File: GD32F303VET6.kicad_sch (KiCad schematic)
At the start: 32 parts, among them SW1 SKRPACE010, U6 GD32F303VCT6, Y1 TAXM8M4RDBCCT2T, Y2 XKXGI-SUA-32.768K

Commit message: 重命名为GD32F303VET6四电机驱动控制板
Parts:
- U6: value GD32F303VCT6 -> GD32F303VET6; footprint kicad_api_lib:GD32F303VCT6 -> kicad_api_lib:GD32F303VET6; symbol GD32F303VCT6:GD32F303VCT6_Mulit -> GD32F303VET6:GD32F303VET6_Mulit

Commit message: 更新六层控制板设计及嘉立创生产文件
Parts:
- removed unit 5 of U6
- renumbered C15 to C16, C16 to C17, C17 to C18, C18 to C19, C19 to C20, C20 to C21, C21 to C22, C22 to C23, C23 to C24, C24 to C25, C25 to C26, C26 to C27, C27 to C28, C28 to C29, C29 to C30, C30 to C31, C31 to C32, C32 to C33, C33 to C34, C34 to C35, D5 to D7, R9 to R11, R10 to R12, R11 to R13, R12 to R14
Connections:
- net DIR2_2 is gone; now on net DIR1_2: U6.34 (DIR2)
- net BRAKE1_1: now also U6.44 (BRAKE1)
- net BRAKE1_2: now also U6.32 (BRAKE2)
- net BRAKE1_3: now also U6.83 (BRAKE3); no longer U6.85 (BRAKE1)
- net BRAKE1_4: now also U6.91 (BRAKE4); no longer U6.87 (BRAKE3)
- net CAN_RX: now also U6.81 (CAN_RX); no longer U6.95 (CAN_RX)
- net CAN_TX: now also U6.82 (CAN_TX); no longer U6.96 (CAN_TX)
- net DIR1_1: now also U6.46 (DIR1)
- net DIR1_3: now also U6.84 (DIR3); no longer U6.86 (BRAKE2)
- net DIR1_4: now also U6.95 (DIR4); no longer U6.88 (BRAKE4)
- net FG1_1: now also U6.45 (TIMER0_CH3-FG1); no longer U6.23 (TIMER1_CH0-FG1)
- net FG1_2: now also U6.42 (TIMER0_CH1-FG2); no longer U6.24 (TIMER1_CH1-FG2)
- net FG1_3: now also U6.90 (TIMER2_CH0-FG3); no longer U6.25 (TIMER1_CH2-FG3)
- net FG1_4: now also U6.96 (TIMER10_CH0-FG4); no longer U6.26 (TIMER1_CH3-FG4)
- net RS485_DE: now also U6.24 (RS485_DE); no longer U6.46 (RS485_DE)
- net RS485_RX: now also U6.26 (RS485_RX); no longer U6.48 (RS485_RX)
- net RS485_TX: now also U6.25 (RS485_TX); no longer U6.47 (RS485_TX)
- net USART0_RX: now also U6.69 (USART0_RX)
- net USART0_TX: now also U6.68 (USART0_TX)
- removed net DIR2_1: U6.33 (DIR1)
- no-connect marks 30 -> 2

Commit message: 更新电机控制板原理图与PCB设计
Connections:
- net FG1_1: now also U6.47 (TIMER1_CH2-FG1); no longer U6.45 (TIMER0_CH3-FG1)
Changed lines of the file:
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@@
 			(alternate "PA3")
 		)
-		(pin "45"
+		(pin "47"
 		)
 		(pin "32"
@@
 		(pin "32"
 		)
-		(pin "45"
+		(pin "47"
 		)
 		(pin "15"
@@
 		(pin "96"
 		)
-		(pin "45"
+		(pin "47"
 		)
 		(pin "62"
@@
 			(alternate "PA3")
 		)
-		(pin "45"
+		(pin "47"
 		)
 		(pin "32"

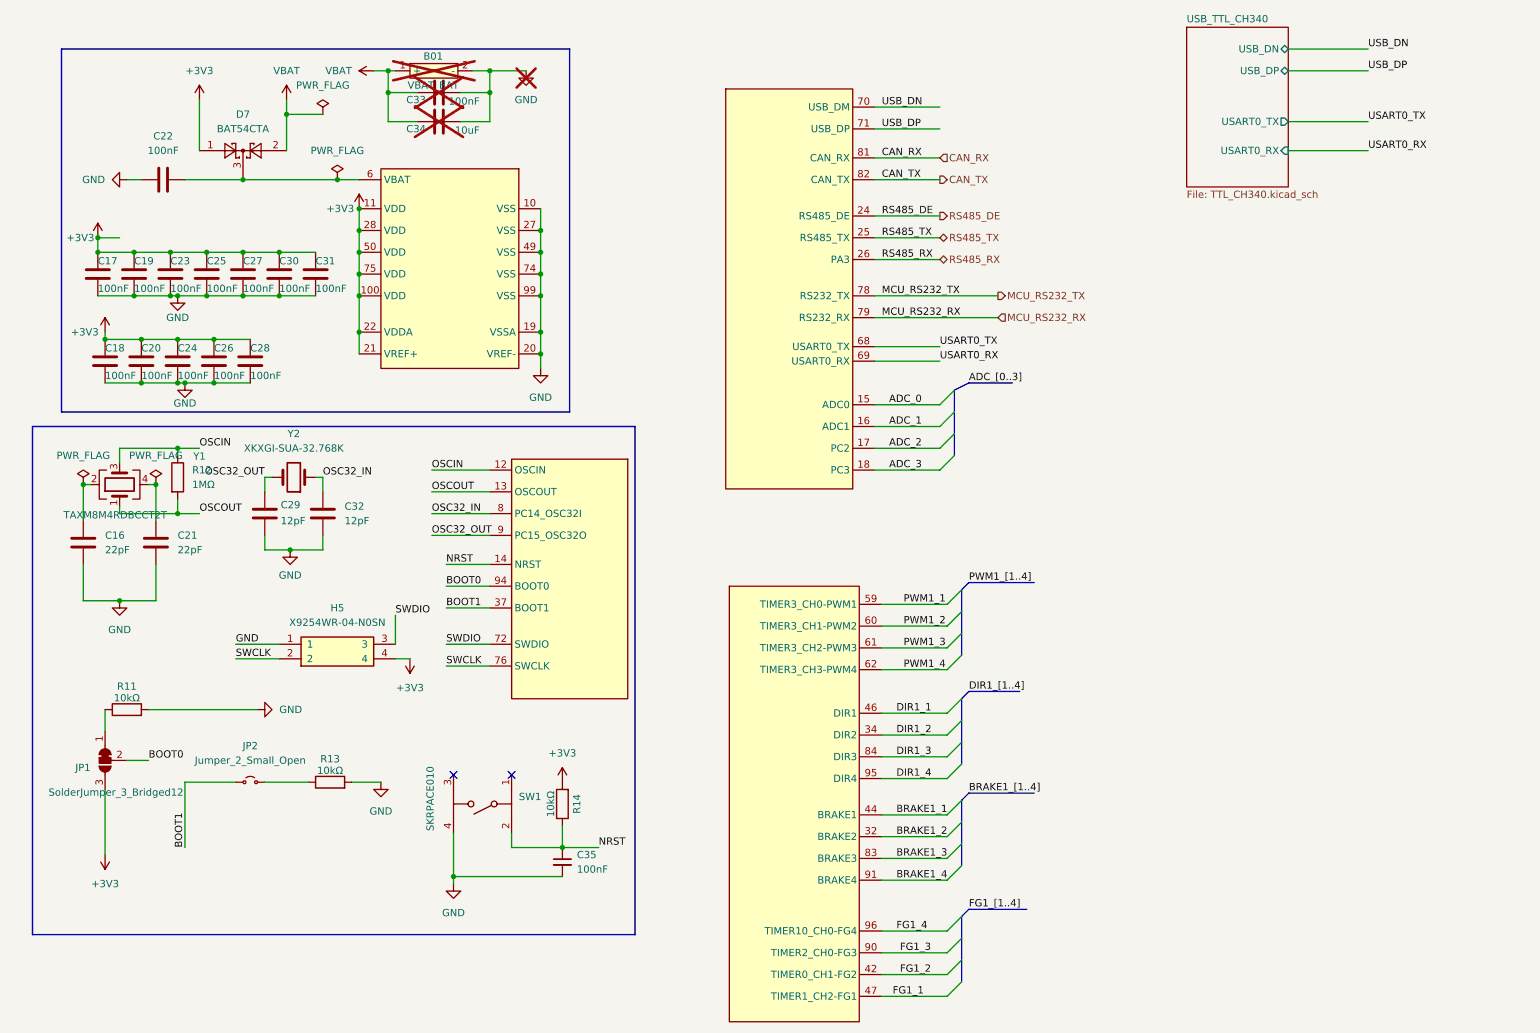
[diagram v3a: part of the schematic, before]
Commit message: 更新六层电机控制板设计与器件库
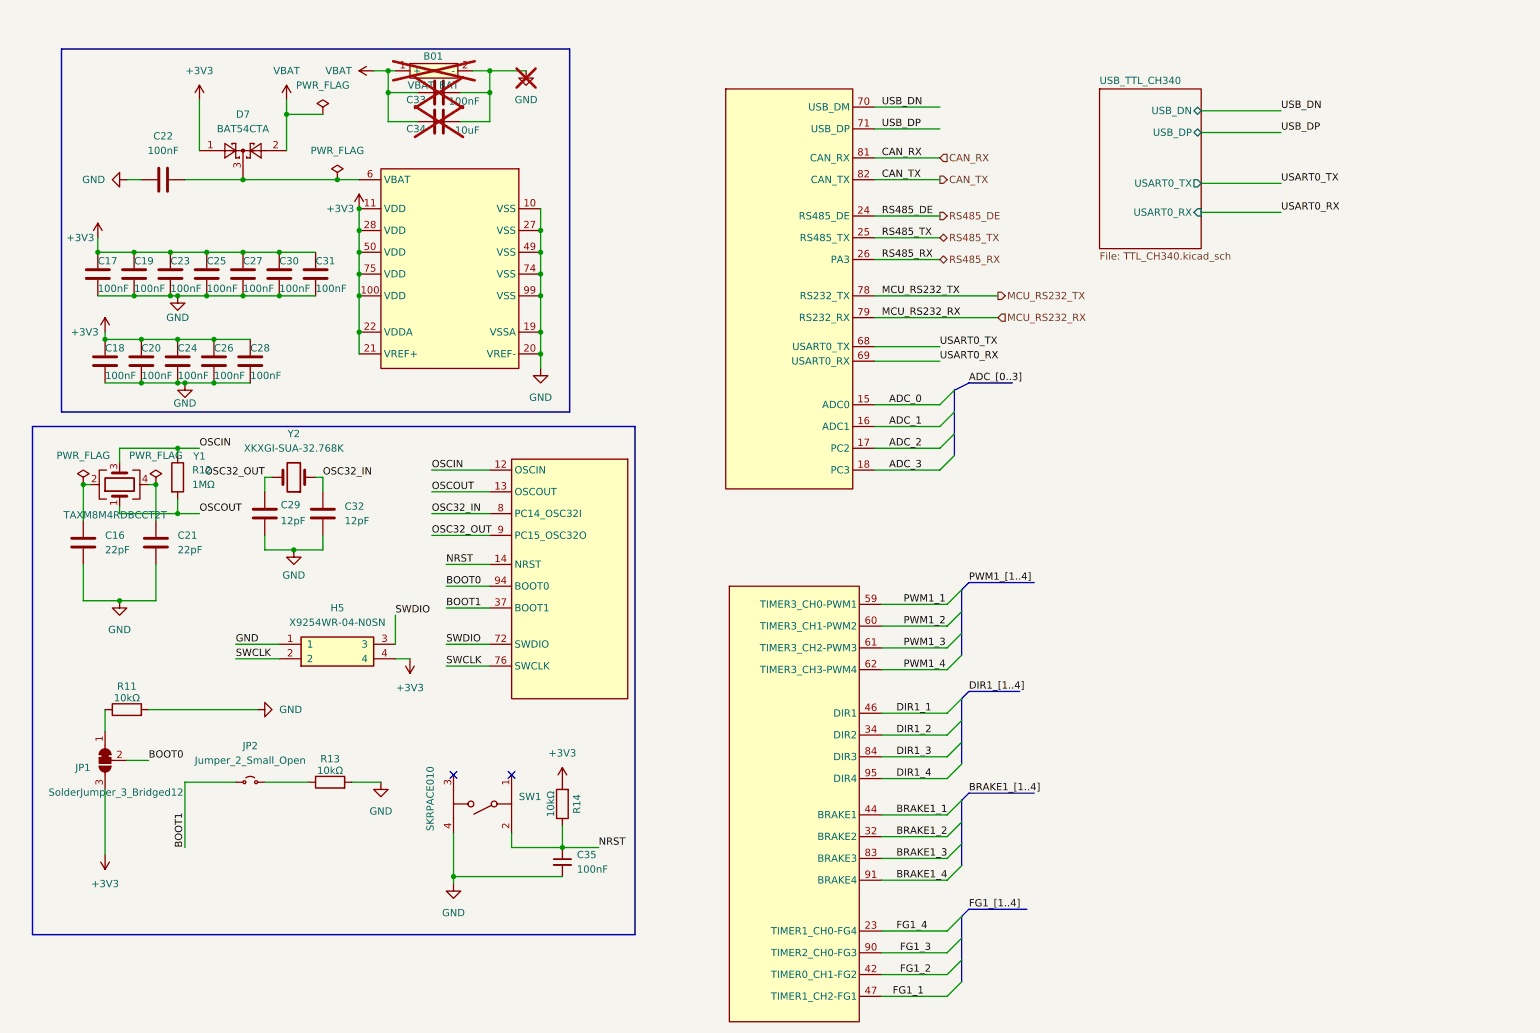
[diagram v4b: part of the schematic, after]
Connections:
- net FG1_4: now also U6.23 (TIMER1_CH0-FG4); no longer U6.96 (TIMER10_CH0-FG4)
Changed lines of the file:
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@@
 	)
 	(junction
+		(at 59.69 113.03)
+		(diameter 0)
+		(color 0 0 0 0)
+	)
+	(junction
 		(at 29.21 121.92)
 		(diameter 0)
@@
 	)
 	(junction
-		(at 25.4 58.42)
-		(diameter 0)
-		(color 0 0 0 0)
-	)
-	(junction
 		(at 93.98 33.02)
 		(diameter 0)
@@
 	)
 	(junction
-		(at 59.055 113.03)
-		(diameter 0)
-		(color 0 0 0 0)
-	)
-	(junction
 		(at 67.31 48.26)
 		(diameter 0)
@@
 	(wire
 		(pts
-			(xy 59.055 113.03) (xy 64.77 113.03)
-		)
-		(stroke
-			(width 0)
-			(type default)
-		)
-	)
-	(wire
-		(pts
 			(xy 34.29 140.97) (xy 53.34 140.97)
 		)
@@
 	(wire
 		(pts
-			(xy 247.65 29.21) (xy 233.68 29.21)
+			(xy 232.41 40.005) (xy 218.44 40.005)
 		)
 		(stroke
@@
 	(wire
 		(pts
-			(xy 54.61 113.03) (xy 59.055 113.03)
+			(xy 54.61 113.03) (xy 59.69 113.03)
 		)
 		(stroke
@@
 	(wire
 		(pts
-			(xy 233.68 25.4) (xy 247.65 25.4)
+			(xy 218.44 36.195) (xy 232.41 36.195)
 		)
 		(stroke
@@
 	(wire
 		(pts
+			(xy 59.69 113.03) (xy 64.77 113.03)
+		)
+		(stroke
+			(width 0)
+			(type default)
+		)
+	)
+	(wire
+		(pts
 			(xy 54.61 153.67) (xy 62.23 153.67)
 		)
@@
 	(wire
 		(pts
-			(xy 233.68 38.1) (xy 247.65 38.1)
+			(xy 218.44 48.895) (xy 232.41 48.895)
 		)
 		(stroke
@@
 	(wire
 		(pts
-			(xy 29.21 58.42) (xy 25.4 58.42)
-		)
-		(stroke
-			(width 0)
-			(type default)
-		)
-	)
-	(wire
-		(pts
 			(xy 87.63 170.18) (xy 106.68 170.18)
 		)
@@
 	(wire
 		(pts
-			(xy 247.65 43.18) (xy 233.68 43.18)
+			(xy 232.41 53.975) (xy 218.44 53.975)
 		)
 		(stroke
@@
 	)
 	(label "USART0_RX"
-		(at 247.65 43.18 0)
+		(at 232.41 53.975 0)
 		(effects
 			(font
@@
 	)
 	(label "USB_DN"
-		(at 247.65 25.4 0)
+		(at 232.41 36.195 0)
 		(effects
 			(font
@@
 	)
 	(label "USB_DP"
-		(at 247.65 29.21 0)
+		(at 232.41 40.005 0)
 		(effects
 			(font
@@
 	)
 	(label "USART0_TX"
-		(at 247.65 38.1 0)
+		(at 232.41 48.895 0)
 		(effects
 			(font
@@
 		(pin "17"
 		)
-		(pin "96"
+		(pin "23"
 		)
 		(pin "42"
@@
 	(symbol
 		(lib_id "power:GND")
-		(at 59.055 113.03 0)
+		(at 59.69 113.03 0)
 		(unit 1)
 		(body_style 1)
@@
 		(fields_autoplaced yes)
 		(property "Reference" "#PWR043"
-			(at 59.055 119.38 0)
+			(at 59.69 119.38 0)
 			(hide yes)
 			(show_name no)
@@
 		)
 		(property "Value" "GND"
-			(at 59.055 117.475 0)
+			(at 59.69 117.475 0)
 			(show_name no)
 			(do_not_autoplace no)
@@
 		)
 		(property "Footprint" ""
-			(at 59.055 113.03 0)
+			(at 59.69 113.03 0)
 			(hide yes)
 			(show_name no)
@@
 		)
 		(property "Datasheet" ""
-			(at 59.055 113.03 0)
+			(at 59.69 113.03 0)
 			(hide yes)
 			(show_name no)
@@
 		)
 		(property "Description" "Power symbol creates a global label with name \"GND\" , ground"
-			(at 59.055 113.03 0)
+			(at 59.69 113.03 0)
 			(hide yes)
 			(show_name no)
@@
 		(pin "70"
 		)
-		(pin "96"
+		(pin "23"
 		)
 		(pin "61"
@@
 		(dnp no)
 		(fields_autoplaced yes)
-		(property "Reference" "#FLG012"
+		(property "Reference" "#FLG013"
 			(at 67.31 46.355 0)
 			(hide yes)
@@
 			(project "GD32F303VET6_4Motor_Control"
 				(path "/54005433-e3aa-4693-8f75-bb73943288d3/ab5b236f-20a8-4993-b87c-2c1c522e6f92"
-					(reference "#FLG012")
+					(reference "#FLG013")
 					(unit 1)
 				)
@@
 		(dnp no)
 		(fields_autoplaced yes)
-		(property "Reference" "#FLG011"
+		(property "Reference" "#FLG012"
 			(at 64.77 34.925 0)
 			(hide yes)
@@
 			(project "GD32F303VET6_4Motor_Control"
 				(path "/54005433-e3aa-4693-8f75-bb73943288d3/ab5b236f-20a8-4993-b87c-2c1c522e6f92"
-					(reference "#FLG011")
+					(reference "#FLG012")
 					(unit 1)
 				)
@@
 		(pin "17"
 		)
-		(pin "96"
+		(pin "23"
 		)
 		(pin "47"
@@
 		(dnp no)
 		(fields_autoplaced yes)
-		(property "Reference" "#FLG09"
+		(property "Reference" "#FLG010"
 			(at 22.86 99.695 0)
 			(hide yes)
@@
 			(project "GD32F303VET6_4Motor_Control"
 				(path "/54005433-e3aa-4693-8f75-bb73943288d3/ab5b236f-20a8-4993-b87c-2c1c522e6f92"
-					(reference "#FLG09")
+					(reference "#FLG010")
 					(unit 1)
 				)
@@
 		(dnp no)
 		(fields_autoplaced yes)
-		(property "Reference" "#FLG010"
+		(property "Reference" "#FLG011"
 			(at 35.56 99.695 0)
 			(hide yes)
@@
 			(project "GD32F303VET6_4Motor_Control"
 				(path "/54005433-e3aa-4693-8f75-bb73943288d3/ab5b236f-20a8-4993-b87c-2c1c522e6f92"
-					(reference "#FLG010")
+					(reference "#FLG011")
 					(unit 1)
 				)
@@
 		(pin "70"
 		)
-		(pin "96"
+		(pin "23"
 		)
 		(pin "61"
@@
 	)
 	(sheet
-		(at 215.9 21.59)
+		(at 200.66 32.385)
 		(size 17.78 27.94)
 		(exclude_from_sim no)
@@
 		)
 		(property "Sheetname" "USB_TTL_CH340"
-			(at 215.9 20.8784 0)
+			(at 200.66 31.6734 0)
 			(show_name no)
 			(do_not_autoplace no)
@@
 		)
 		(property "Sheetfile" "TTL_CH340.kicad_sch"
-			(at 215.9 50.1146 0)
+			(at 200.66 60.9096 0)
 			(show_name no)
 			(do_not_autoplace no)
@@
 		)
 		(pin "USB_DN" bidirectional
-			(at 233.68 25.4 0)
+			(at 218.44 36.195 0)
 			(effects
 				(font
@@
 		)
 		(pin "USB_DP" bidirectional
-			(at 233.68 29.21 0)
+			(at 218.44 40.005 0)
 			(effects
 				(font
@@
 		)
 		(pin "USART0_TX" output
-			(at 233.68 38.1 0)
+			(at 218.44 48.895 0)
 			(effects
 				(font
@@
 		)
 		(pin "USART0_RX" input
-			(at 233.68 43.18 0)
+			(at 218.44 53.975 0)
 			(effects
 				(font

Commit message: 更新电源与USB供电设计、PCB及器件库
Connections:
- net GND: now also Y1.2 (GND), Y1.4 (GND)
- net OSCIN: now also C16.2
- net OSCOUT: now also C21.2
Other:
- moved on the sheet: C21

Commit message: V2.0: sync KiCad design, add firmware snapshot and README
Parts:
- added C40: 100nF, Capacitor_SMD:C_0603_1608Metric, symbol Device:C_Small
- added R18, R19, R20: 10kΩ, Resistor_SMD:R_0603_1608Metric, symbol Device:R
- added unit 5 of U7
- added U8: GD25Q16ESIGR, kicad_api_lib:GD25Q16ESIGR, symbol GD25Q16ESIGR:GD25Q32CTIGR
- C20: renamed from C16; value 22pF -> 15pF; footprint Capacitor_SMD:C_0603_1608Metric_Pad1.08x0.95mm_HandSolder -> Capacitor_SMD:C_0603_1608Metric
- C25: renamed from C21; value 22pF -> 15pF
- C33: renamed from C29; value 12pF -> 15pF
- C36: renamed from C32; value 12pF -> 15pF
- C37: renamed from C33; value 100nF -> C
- C38: renamed from C34; value 10uF -> C
- H5: footprint Connector_PinHeader_2.54mm:PinHeader_1x04_P2.54mm_Vertical -> kicad_api_lib:X9254WR-04-N0SN
- JP1: footprint Jumper:SolderJumper-3_P1.3mm_Bridged12_RoundedPad1.0x1.5mm -> (none)
- JP2: footprint Connector_PinHeader_2.54mm:PinHeader_1x02_P2.54mm_Vertical -> (none)
- R14: renamed from R11; footprint Resistor_SMD:R_0603_1608Metric_Pad0.98x0.95mm_HandSolder -> Resistor_SMD:R_0603_1608Metric
- R15: renamed from R12; footprint Resistor_SMD:R_0603_1608Metric_Pad0.98x0.95mm_HandSolder -> Resistor_SMD:R_0603_1608Metric
- R16: renamed from R13; footprint Resistor_SMD:R_0603_1608Metric_Pad0.98x0.95mm_HandSolder -> Resistor_SMD:R_0603_1608Metric
- R17: renamed from R14; footprint Resistor_SMD:R_0603_1608Metric_Pad0.98x0.95mm_HandSolder -> Resistor_SMD:R_0603_1608Metric
- renumbered C17 to C21, C18 to C22, C19 to C23, C20 to C24, C22 to C26, C23 to C27, C24 to C28, C25 to C29, C26 to C30, C27 to C31, C28 to C32, C30 to C34, C31 to C35, C35 to C39, D7 to D8, U6 to U7
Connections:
- net +3V3: now also C40.1, R18.2, R19.1, R20.1, U8.8 (VCC); no longer H5.4
- net GND renamed +BATT
- net +BATT: now also C37.2, C38.2, C40.2, U8.4 (VSS)
- removed net VBAT: C37.2, C38.2, D8.2
- new net: R20.2, U8.7 (HOLD#(IO3))
- new net: R19.2, U8.3 (WP#(IO2))
- new net +5V: H5.4
- new net MCU_SPI_MISO: U7.53 (PB14/SPI1_MISO/USART2_RTS/TIMER0_CH1_ON), U8.2 (SO(IO1))
- new net MCU_SPI_MOSI: U7.54 (PB15/SPI1_MOSI/TIMER0_CH2_ON/I2S1_SD), U8.5 (SI(IO0))
- new net MCU_SPI_NSS: R18.1, U7.51 (PB12/SPI1_NSS/I2C1_SMBA/USART2_CK/TIMER0_BRKIN/I2S1_WS), U8.1 (CS#)
- new net MCU_SPI_SLK: U7.52 (PB13/SPI1_SCK/USART2_CTS/TIMER0_CH0_ON/I2S1_CK), U8.6 (SCLK)
- new net Motor_start: U7.58 (PD11/EXMC_A16)
- new net VCC: D8.2
- no-connect marks 2 -> 41
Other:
- sheet Motor_Comm ports: added Motor_start; removed none
- note added: "MCU-01 供电与去耦"
- note added: "MCU-01｜+3V3 供电与各电源引脚旁路。 D8 为 VBAT 供电选择支路。 B01 / C37 / C38 为备用区域，当前 DNP。 MCU-02｜Y1：主时钟；Y2：低速时钟。 JP1 / JP2：BOOT 配置；SW1：手动复位。 R17 / C39：NRST 上拉与滤波。 H5：SWD 下载 / 调试接口。 MCU-05｜U8：GD25Q16 SPI Flash。 R18 / R19 / R20 保持控制脚默认电平；C40 去耦。 MCU-06｜Motor_start 输出至电机页 U15.OE。 高电平允许 PWM 电平转换；低电平关闭。 此处没有硬件锁存，需 MCU 持续维持使能。 MCU-07｜PWM1、DIR1、BRAKE1 为控制输出； FG1 为测速输入，按电机通道编号对应。"
- note added: "MCU-02 时钟 / 启动 / 调试"
- note added: "MCU-03 通信与 ADC 引脚"
- note added: "MCU-04 USB / 电机子页接口"
- note added: "MCU-05 SPI 非易失存储"
- note added: "MCU-06 扩展 GPIO 与总使能"
- note added: "MCU-07 四路电机控制与测速"
- note added: "接口命名说明：MCU_SPI_SLK 保留现有名称，实际连接 Flash 的 SCLK。 Motor_start 控制 PWM 通道使能；它不直接表示电机正在转动。"

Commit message: V2.0: update motor control schematics, replicated PCB layout and component libraries
Save current KiCad design progress, including four motor control layouts and new component libraries. PCB routing and DRC cleanup remain unfinished; this is not a fabrication release.
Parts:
- added U26, U27: ESP32-C3-WROOM-02U-N4, kicad_api_lib:ESP32-C3-WROOM-02U-N4, symbol ESP32-C3-WROOM-02U-N4:ESP32-C3-WROOM-02U-N4
- D8: now not fitted; now left out of the parts list
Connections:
- net +3V3: now also C26.1, D8.3, U7.6 (VBAT)
- net BRAKE1_2: now also U7.33 (PC4/ADC01_IN14); no longer U7.32 (PA7/SPI0_MOSI/ADC01_IN7/TIMER2_CH1/TIMER7_CH0_ON)
- net MCU_SPI_MISO: now also U7.31 (PA6/SPI0_MISO/ADC01_IN6/TIMER2_CH0/TIMER7_BRKIN); no longer U7.53 (PB14/SPI1_MISO/USART2_RTS/TIMER0_CH1_ON)
- net MCU_SPI_MOSI: now also U7.32 (PA7/SPI0_MOSI/ADC01_IN7/TIMER2_CH1/TIMER7_CH0_ON); no longer U7.54 (PB15/SPI1_MOSI/TIMER0_CH2_ON/I2S1_SD)
- net MCU_SPI_NSS: now also U7.29 (PA4/SPI0_NSS/USART1_CK/ADC01_IN4/DAC_OUT); no longer U7.51 (PB12/SPI1_NSS/I2C1_SMBA/USART2_CK/TIMER0_BRKIN/I2S1_WS)
- net MCU_SPI_SLK: now also U7.30 (PA5/SPI0_SCK/ADC01_IN5/DAC0_OUT1); no longer U7.52 (PB13/SPI1_SCK/USART2_CTS/TIMER0_CH0_ON/I2S1_CK)
